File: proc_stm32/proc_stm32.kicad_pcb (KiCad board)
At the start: 2 copper layers, 21.8 x 18.8 mm, 7 parts, among them J1 Moat_Compute_24, U2 STM32L051K8Tx

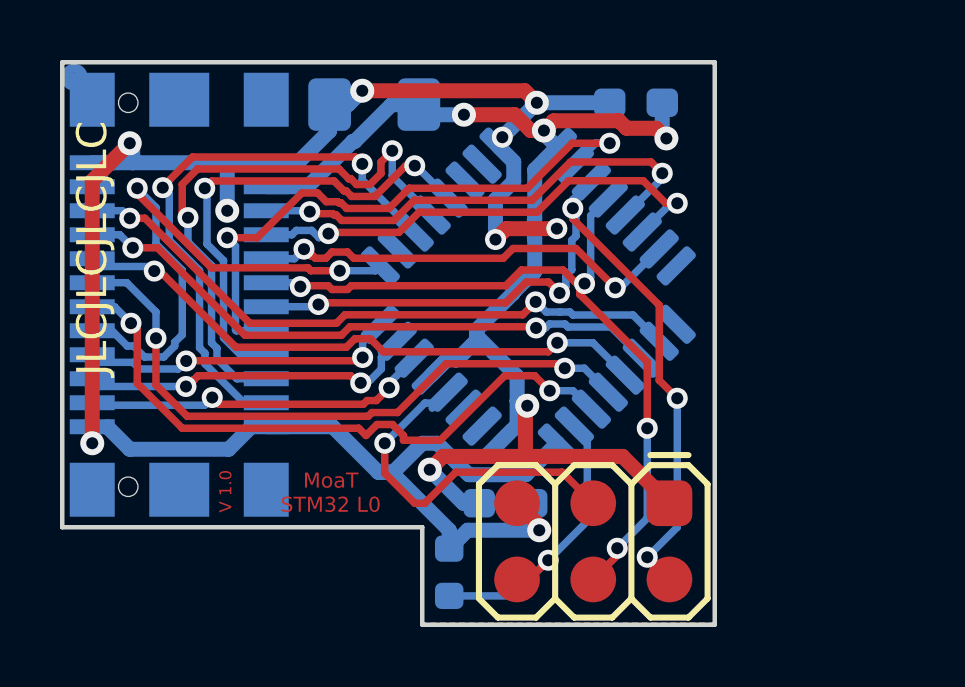
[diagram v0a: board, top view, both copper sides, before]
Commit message: Plug updates
drop in/out from plug24
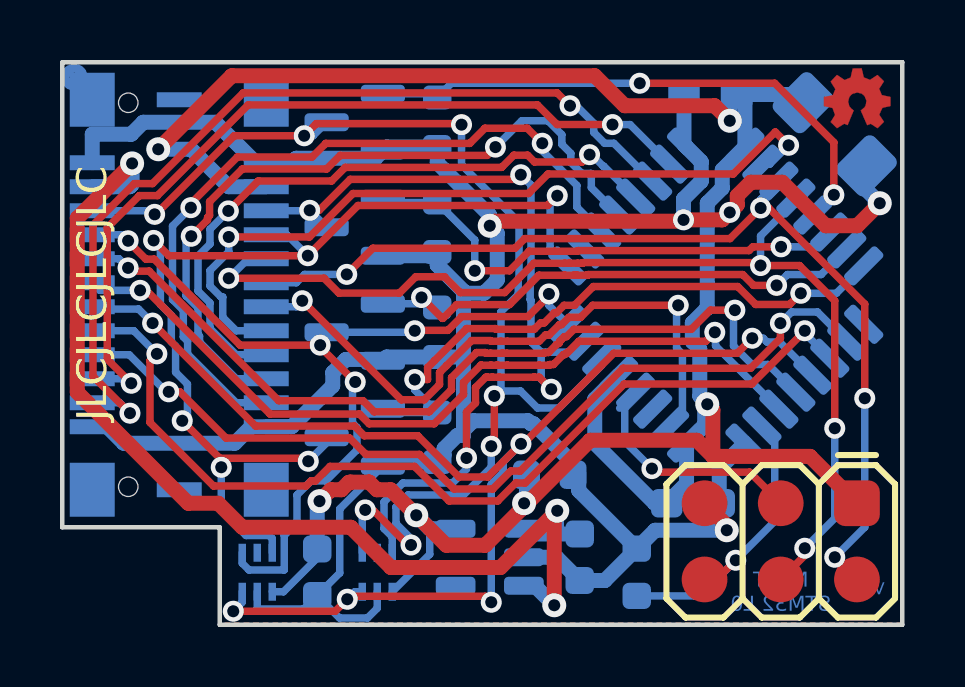
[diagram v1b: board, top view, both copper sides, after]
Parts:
- added C4: 1µ, Capacitor_SMD:C_0603_1608Metric, B.Cu at (52.8, 61.0)
- added C5: 1µ, Capacitor_SMD:C_0603_1608Metric, B.Cu at (51.8, 58.2)
- added C6: 100n, Capacitor_SMD:C_0603_1608Metric, B.Cu at (44.0, 61.5)
- added G***: LOGO, localstuff:OSHW Logo 2mm Cu, F.Cu at (62.0, 45.7)
- added Q1: 2N7002, Package_TO_SOT_SMD:SOT-23, B.Cu at (45.2, 46.5)
- added Q2: 2N7002, Package_TO_SOT_SMD:SOT-23, B.Cu at (45.2, 50.0)
- added Q3: 2N7002, Package_TO_SOT_SMD:SOT-23, B.Cu at (45.2, 53.5)
- added Q4: 2N7002, Package_TO_SOT_SMD:SOT-23, B.Cu at (45.2, 57.0)
- added R2: 1M, Resistor_SMD:R_0603_1608Metric, B.Cu at (48.0, 46.5)
- added R3: 1M, Resistor_SMD:R_0603_1608Metric, B.Cu at (48.0, 50.0)
- added R4: 1M, Resistor_SMD:R_0603_1608Metric, B.Cu at (48.0, 53.5)
- added R5: 1M, Resistor_SMD:R_0603_1608Metric, B.Cu at (48.0, 57.0)
- added U1: MIC5504, Package_TO_SOT_SMD:SOT-23-5, B.Cu at (49.8, 61.0)
- added U3: LTC4311, Package_DFN_QFN:ST_UQFN-6L_1.5x1.7mm_Pitch0.5mm, B.Cu at (46.0, 61.5)
- added U4: LTC4311, Package_DFN_QFN:ST_UQFN-6L_1.5x1.7mm_Pitch0.5mm, B.Cu at (42.0, 61.5)
- moved C3 15.4 mm to (61.2, 46.9), turned to -45 degrees
- moved C2 6.25 mm to (56.5, 59.2)
- moved Prog1 6.25 mm to (59.5, 60.5)
- moved R1 6.25 mm to (54.6, 61.5)
- moved U2 6.25 mm to (57.3, 52.3)
- moved C1 2.49 mm to (57.1, 45.6)
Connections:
- J1 pad 10: /Bus3_out -> /Rx
- J1 pad 11: /SCLx -> /SDAx
- J1 pad 12: /Rx -> /Tx
- J1 pad 13: /SDAx -> /ena
- J1 pad 14: /Tx -> /1wire
- J1 pad 15: /1wire -> /SW4
- J1 pad 5: /Bus1_in -> /Bus1
- J1 pad 6: /Bus1_out -> /Bus2
- J1 pad 7: /Bus2_in -> /Bus3
- J1 pad 8: /Bus2_out -> /Bus4
- J1 pad 9: /Bus3_in -> /SCLx
- U2 pad 14: unconnected-(U2-Pad14) -> /SW1
- U2 pad 15: unconnected-(U2-Pad15) -> /SW2
- U2 pad 2: unconnected-(U2-Pad2) -> /1wire
- U2 pad 24: unconnected-(U2-Pad24) -> /Bus4_out
- U2 pad 26: /Bus1_in -> /SW3
- U2 pad 27: /Bus2_in -> /SW4
- U2 pad 28: /Bus3_in -> /ena
- U2 pad 6: /SW1 -> /Bus1
- U2 pad 7: /SW2 -> /Bus2
- U2 pad 8: /SW3 -> /Bus3
- U2 pad 9: /1wire -> /Bus4
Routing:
- net /ena: track 0.00 -> 44.8 mm, vias 0 -> 6
- net /Bus1: track 0.00 -> 40.3 mm, vias 0 -> 7
- net +3V3: track 44.2 -> 81.4 mm, vias 5 -> 6
- net +5V: track 0.00 -> 36.8 mm, vias 0 -> 3
- net /Bus4: track 0.00 -> 35.5 mm, vias 0 -> 6
- net GND: track 66.3 -> 98.3 mm, vias 9 -> 5
- net /SW4: track 0.00 -> 31.9 mm, vias 0 -> 2
- net /Bus3: track 0.00 -> 30.1 mm, vias 0 -> 5
- net /Bus2: track 0.00 -> 29.7 mm, vias 0 -> 4
- net /Bus1_in: track 21.3 -> 0.00 mm, vias 2 -> 0
- net /Bus4_out: track 0.00 -> 20.6 mm, vias 0 -> 2
- net /Bus2_in: track 20.4 -> 0.00 mm, vias 2 -> 0
- net /Bus3_in: track 19.9 -> 0.00 mm, vias 2 -> 0
- net /SW3: track 10.7 -> 30.1 mm
- net /SW1: track 11.7 -> 30.1 mm
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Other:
- board size 21.8 x 18.8 mm -> 28 x 18.8 mm
- board text added: "V 2.3"
- board text removed: "V 1.0"

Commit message: uploads
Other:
- rule pad_to_mask_clearance: 0.051 -> 0
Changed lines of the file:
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@@
 (kicad_pcb (version 20211014) (generator pcbnew)
   (general
-    (thickness 1.6)
+    (thickness 1.09)
   )
   (paper "A4")
@@
   (setup
     (stackup
-      (layer "F.SilkS" (type "Top Silk Screen"))
+      (layer "F.SilkS" (type "Top Silk Screen") (color "White"))
       (layer "F.Paste" (type "Top Solder Paste"))
       (layer "F.Mask" (type "Top Solder Mask") (color "Green") (thickness 0.01))
       (layer "F.Cu" (type "copper") (thickness 0.035))
-      (layer "dielectric 1" (type "core") (thickness 1.51) (material "FR4") (epsilon_r 4.5) (loss_tangent 0.02))
+      (layer "dielectric 1" (type "core") (thickness 1) (material "FR4") (epsilon_r 4.5) (loss_tangent 0.02))
       (layer "B.Cu" (type "copper") (thickness 0.035))
       (layer "B.Mask" (type "Bottom Solder Mask") (color "Green") (thickness 0.01))
       (layer "B.Paste" (type "Bottom Solder Paste"))
-      (layer "B.SilkS" (type "Bottom Silk Screen"))
+      (layer "B.SilkS" (type "Bottom Silk Screen") (color "White"))
       (copper_finish "None")
       (dielectric_constraints no)
     )
-    (pad_to_mask_clearance 0.051)
-    (solder_mask_min_width 0.25)
+    (pad_to_mask_clearance 0)
     (grid_origin 145 137.2)
     (pcbplotparams
@@
   (segment (start 49.999501 51.760455) (end 49.560455 52.199501) (width 0.5) (layer "B.Cu") (net 1))
   (segment (start 44.516334 54.846487) (end 44.95538 54.407441) (width 0.5) (layer "B.Cu") (net 1))
+  (segment (start 36.5 47.85) (end 36.5 47) (width 0.5) (layer "B.Cu") (net 1))
   (segment (start 56.225 45.575) (end 56.225 47.243629) (width 0.5) (layer "B.Cu") (net 1))
   (segment (start 56.800509 48.466476) (end 56.208976 49.058009) (width 0.5) (layer "B.Cu") (net 1))
@@
   (segment (start 52.716492 58.778992) (end 52.716492 58.166492) (width 0.5) (layer "B.Cu") (net 1))
   (segment (start 44.74952 59.38798) (end 46.1875 57.95) (width 0.25) (layer "B.Cu") (net 1))
-  (segment (start 38.2 46.5) (end 40.600978 46.5) (width 0.5) (layer "B.Cu") (net 1))
+  (segment (start 36.5 47) (end 37.7 47) (width 0.5) (layer "B.Cu") (net 1))
   (segment (start 43.35 47.85) (end 42.3 47.85) (width 0.5) (layer "B.Cu") (net 1))
   (segment (start 55.2625 60.1) (end 54.65 60.7125) (width 0.5) (layer "B.Cu") (net 1))
@@
   (segment (start 44 62.275) (end 44.74952 61.52548) (width 0.25) (layer "B.Cu") (net 1))
   (segment (start 51.124062 56.549011) (end 51.02555 56.450499) (width 0.5) (layer "B.Cu") (net 1))
-  (segment (start 36.5 47.85) (end 36.5 46.900511) (width 0.5) (layer "B.Cu") (net 1))
   (segment (start 57.4 58.050001) (end 58.255888 57.194113) (width 0.5) (layer "B.Cu") (net 1))
   (segment (start 42.024511 62.724511) (end 43.550489 62.724511) (width 0.25) (layer "B.Cu") (net 1))
@@
   (segment (start 52.525 57.865044) (end 51.208968 56.549012) (width 0.5) (layer "B.Cu") (net 1))
   (segment (start 46.3125 57.825) (end 46.1875 57.95) (width 0.5) (layer "B.Cu") (net 1))
+  (segment (start 40.600978 46.5) (end 41.950978 47.85) (width 0.5) (layer "B.Cu") (net 1))
   (segment (start 62.301821 48.751821) (end 62.75 49.2) (width 0.5) (layer "B.Cu") (net 1))
   (segment (start 49.198541 56.450499) (end 48.87452 56.77452) (width 0.5) (layer "B.Cu") (net 1))
@@
   (segment (start 49.999501 50.199501) (end 49.75 49.95) (width 0.5) (layer "B.Cu") (net 1))
   (segment (start 46 62.7) (end 45.675499 63.024501) (width 0.25) (layer "B.Cu") (net 1))
-  (segment (start 36.5 46.900511) (end 37.799489 46.900511) (width 0.5) (layer "B.Cu") (net 1))
-  (segment (start 37.799489 46.900511) (end 38.2 46.5) (width 0.5) (layer "B.Cu") (net 1))
   (segment (start 45.57629 54.407441) (end 45.618849 54.45) (width 0.5) (layer "B.Cu") (net 1))
   (segment (start 46.1875 50.95) (end 47.875 50.95) (width 0.5) (layer "B.Cu") (net 1))
@@
   (segment (start 57.65 60.1) (end 55.2625 60.1) (width 0.5) (layer "B.Cu") (net 1))
   (segment (start 49.999501 51.760455) (end 49.999501 50.199501) (width 0.5) (layer "B.Cu") (net 1))
-  (segment (start 40.600978 46.5) (end 41.950978 47.85) (width 0.5) (layer "B.Cu") (net 1))
   (segment (start 48 51.009956) (end 48 50.825) (width 0.5) (layer "B.Cu") (net 1))
   (segment (start 54.65 60.7125) (end 52.716492 58.778992) (width 0.5) (layer "B.Cu") (net 1))
@@
   (segment (start 56.225 47.243629) (end 56.311344 47.329973) (width 0.5) (layer "B.Cu") (net 1))
   (segment (start 42.3 56.65) (end 43.147862 56.65) (width 0.5) (layer "B.Cu") (net 1))
-  (segment (start 41.950978 47.85) (end 42.3 47.85) (width 0.5) (layer "B.Cu") (net 1))
   (segment (start 37.55 57.2) (end 41.25 57.2) (width 0.5) (layer "B.Cu") (net 1))
   (segment (start 37 56.65) (end 37.55 57.2) (width 0.5) (layer "B.Cu") (net 1))
   (segment (start 41.25 57.2) (end 41.8 56.65) (width 0.5) (layer "B.Cu") (net 1))
+  (segment (start 37.7 47) (end 38.2 46.5) (width 0.5) (layer "B.Cu") (net 1))
+  (segment (start 38.2 46.5) (end 40.600978 46.5) (width 0.5) (layer "B.Cu") (net 1))
   (segment (start 48.87452 56.941882) (end 48.87452 54.32548) (width 0.5) (layer "B.Cu") (net 1))
   (segment (start 46.3125 54.325) (end 48 54.325) (width 0.5) (layer "B.Cu") (net 1))
@@
   (segment (start 44 62.283179) (end 44 62.275) (width 0.25) (layer "B.Cu") (net 1))
   (segment (start 57.4 59.2) (end 57.4 59.85) (width 0.5) (layer "B.Cu") (net 1))
+  (segment (start 41.950978 47.85) (end 42.3 47.85) (width 0.5) (layer "B.Cu") (net 1))
   (segment (start 48.665104 56.941882) (end 48.87452 56.941882) (width 0.5) (layer "B.Cu") (net 1))
   (segment (start 49.901978 57.198022) (end 49.901978 55.622552) (width 0.25) (layer "F.Cu") (net 2))

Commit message: No save for too long …
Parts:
- C4, C5: value 1µ -> 1µF
- C6: value 100n -> 100nF
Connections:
- U1 pad 4: (no net) -> unconnected-(U1-NC)
- U3 pad 5: (no net) -> unconnected-(U3-NC)
- U4 pad 5: (no net) -> unconnected-(U4-NC)

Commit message: de-JLC
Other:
- board text removed: "JLCJLCJLCJLC"
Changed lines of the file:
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@@
     (effects (font (size 0.5 0.5) (thickness 0.1)) (justify mirror))
-  )
-  (gr_text "JLCJLCJLCJLC\n" (at 36.5 52.2 90) (layer "F.SilkS")
-    (effects (font (size 1 1) (thickness 0.15)))
   )
   (segment (start 57.749768 49.505347) (end 58 49.255115) (width 0.5) (layer "F.Cu") (net 1))
